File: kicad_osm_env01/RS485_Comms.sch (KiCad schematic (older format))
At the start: 13 parts, among them U7 ST3485EBDR

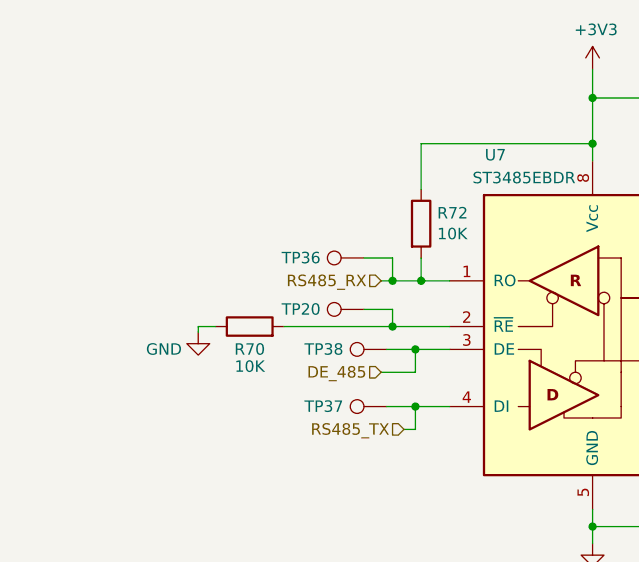
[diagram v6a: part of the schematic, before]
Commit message: updated schematics
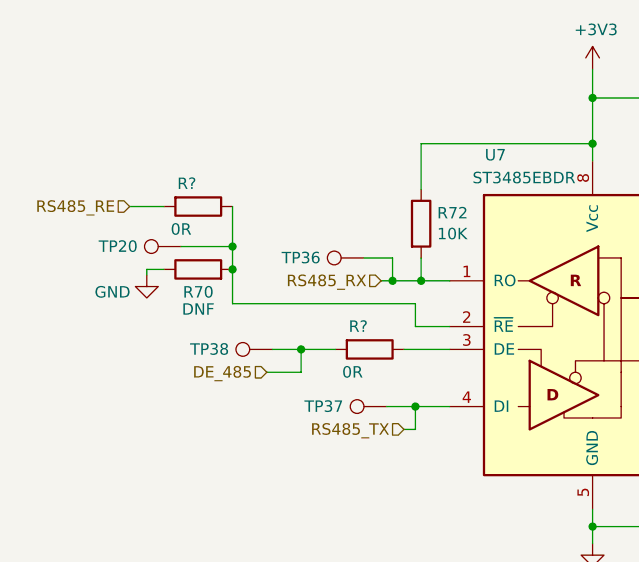
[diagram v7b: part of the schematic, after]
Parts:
- added R? (x2): 0R, symbol device:R
- R70: value 10K -> DNF
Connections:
- net DE_485: now also R?.2; no longer U7.3 (DE)
- net at R70.2, TP20.1, U7.2 (~RE): now also R?.1
- new net: R?.1, U7.3 (DE)
- new net RS485_RE: R?.2
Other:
- moved on the sheet: R70, TP20, TP38
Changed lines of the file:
@@
 L OSM_env01-rescue:R-device-ESP32-EVB_Rev_D-rescue R?
 U 1 1 609E7D1E
-P 4150 3825
+P 3925 3575
 AR Path="/609E7D1E" Ref="R?"  Part="1"
 AR Path="/609D4B87/609E7D1E" Ref="R70"  Part="1"
-F 0 "R70" V 4050 3825 50  0000 C CNN
-F 1 "10K" V 3975 3825 50  0000 C CNN
-F 2 "Resistor_SMD:R_0603_1608Metric" V 4080 3825 50  0001 C CNN
-F 3 "" H 4150 3825 50  0001 C CNN
-	1    4150 3825
+F 0 "R70" V 3825 3575 50  0000 C CNN
+F 1 "DNF" V 3750 3575 50  0000 C CNN
+F 2 "Resistor_SMD:R_0603_1608Metric" V 3855 3575 50  0001 C CNN
+F 3 "" H 3925 3575 50  0001 C CNN
+	1    3925 3575
 	0    -1   -1   0
 $EndComp
@@
 L OSM_env01-rescue:GND-ESP32-EVB_Rev_D #PWR?
 U 1 1 609E7D6C
-P 3925 3850
+P 3700 3600
 AR Path="/609E7D6C" Ref="#PWR?"  Part="1"
 AR Path="/609D4B87/609E7D6C" Ref="#PWR054"  Part="1"
-F 0 "#PWR054" H 3925 3600 50  0001 C CNN
-F 1 "GND" H 3775 3775 50  0000 C CNN
-F 2 "" H 3925 3850 60  0000 C CNN
-F 3 "" H 3925 3850 60  0000 C CNN
-	1    3925 3850
-	1    0    0    -1
-$EndComp
-Wire Wire Line
-	3925 3850 3925 3825
-Wire Wire Line
-	3925 3825 4000 3825
+F 0 "#PWR054" H 3700 3350 50  0001 C CNN
+F 1 "GND" H 3550 3525 50  0000 C CNN
+F 2 "" H 3700 3600 60  0000 C CNN
+F 3 "" H 3700 3600 60  0000 C CNN
+	1    3700 3600
+	1    0    0    -1
+$EndComp
+Wire Wire Line
+	3700 3600 3700 3575
+Wire Wire Line
+	3700 3575 3775 3575
 Wire Wire Line
 	4900 3025 5650 3025
@@
 L OSM_env01-rescue:Test_Point-Connector-ESP32-EVB_Rev_D-rescue TP?
 U 1 1 609E7D92
-P 4750 3925
+P 4250 3925
 AR Path="/609E7D92" Ref="TP?"  Part="1"
 AR Path="/609D4B87/609E7D92" Ref="TP38"  Part="1"
-F 0 "TP38" V 4750 4200 50  0000 C CNN
-F 1 "Test_Point" V 4675 4300 50  0001 C CNN
-F 2 "TestPoint:TestPoint_Pad_D1.5mm" H 4950 3925 50  0001 C CNN
-F 3 "~" H 4950 3925 50  0001 C CNN
-	1    4750 3925
+F 0 "TP38" V 4250 4200 50  0000 C CNN
+F 1 "Test_Point" V 4175 4300 50  0001 C CNN
+F 2 "TestPoint:TestPoint_Pad_D1.5mm" H 4450 3925 50  0001 C CNN
+F 3 "~" H 4450 3925 50  0001 C CNN
+	1    4250 3925
 	0    -1   -1   0
 $EndComp
@@
 Wire Wire Line
 	6950 4100 7025 4100
-Text HLabel 4725 4025 0    50   Input ~ 0
+Text HLabel 4225 4025 0    50   Input ~ 0
 DE_485
 Text HLabel 4725 3625 0    50   Input ~ 0
@@
 	4875 4175 5025 4175
 Wire Wire Line
-	4300 3825 4775 3825
-Wire Wire Line
-	4750 3925 4875 3925
-Wire Wire Line
-	4875 3925 4875 4025
-Wire Wire Line
-	4875 4025 4725 4025
-Connection ~ 4875 3925
-Wire Wire Line
-	4875 3925 5025 3925
+	4250 3925 4375 3925
+Wire Wire Line
+	4375 3925 4375 4025
+Wire Wire Line
+	4375 4025 4225 4025
+Connection ~ 4375 3925
+Wire Wire Line
+	4375 3925 4525 3925
 Text HLabel 4825 4275 0    50   Input ~ 0
 RS485_TX
@@
 L OSM_env01-rescue:Test_Point-Connector-ESP32-EVB_Rev_D-rescue TP?
 U 1 1 61C934C6
-P 4650 3750
+P 3850 3475
 AR Path="/61C934C6" Ref="TP?"  Part="1"
 AR Path="/609D4B87/61C934C6" Ref="TP20"  Part="1"
-F 0 "TP20" V 4650 4025 50  0000 C CNN
-F 1 "Test_Point" V 4775 4125 50  0001 C CNN
-F 2 "TestPoint:TestPoint_Pad_D1.5mm" H 4850 3750 50  0001 C CNN
-F 3 "~" H 4850 3750 50  0001 C CNN
-	1    4650 3750
-	0    -1   -1   0
-$EndComp
-Wire Wire Line
-	4650 3750 4775 3750
-Wire Wire Line
-	4775 3750 4775 3825
-Connection ~ 4775 3825
-Wire Wire Line
-	4775 3825 5025 3825
+F 0 "TP20" V 3850 3750 50  0000 C CNN
+F 1 "Test_Point" V 3975 3850 50  0001 C CNN
+F 2 "TestPoint:TestPoint_Pad_D1.5mm" H 4050 3475 50  0001 C CNN
+F 3 "~" H 4050 3475 50  0001 C CNN
+	1    3850 3475
+	0    -1   -1   0
+$EndComp
+Text HLabel 3625 3300 0    50   Input ~ 0
+RS485_RE
+Wire Wire Line
+	3775 3300 3625 3300
+Wire Wire Line
+	3850 3475 4075 3475
+Connection ~ 4075 3475
+$Comp
+L device:R R?
+U 1 1 614C78FA
+P 4675 3925
+AR Path="/6064BC1D/614C78FA" Ref="R?"  Part="1"
+AR Path="/609D4B87/614C78FA" Ref="R?"  Part="1"
+F 0 "R?" V 4575 3875 50  0000 C CNN
+F 1 "0R" V 4775 3850 50  0000 C CNN
+F 2 "" V 4605 3925 50  0001 C CNN
+F 3 "" H 4675 3925 50  0001 C CNN
+	1    4675 3925
+	0    1    1    0
+$EndComp
+$Comp
+L device:R R?
+U 1 1 614D39E0
+P 3925 3300
+AR Path="/6064BC1D/614D39E0" Ref="R?"  Part="1"
+AR Path="/609D4B87/614D39E0" Ref="R?"  Part="1"
+F 0 "R?" V 3825 3250 50  0000 C CNN
+F 1 "0R" V 4025 3225 50  0000 C CNN
+F 2 "" V 3855 3300 50  0001 C CNN
+F 3 "" H 3925 3300 50  0001 C CNN
+	1    3925 3300
+	0    1    1    0
+$EndComp
+Wire Wire Line
+	4075 3475 4075 3575
+Wire Wire Line
+	4075 3300 4075 3475
+Wire Wire Line
+	5025 3925 4825 3925
+Wire Wire Line
+	5025 3825 4875 3825
+Wire Wire Line
+	4875 3825 4875 3725
+Wire Wire Line
+	4075 3725 4075 3575
+Wire Wire Line
+	4075 3725 4875 3725
+Connection ~ 4075 3575
 $EndSCHEMATC

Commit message: updated schematics
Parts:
- gave numbers to parts that had none: 2
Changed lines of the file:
@@
 P 4675 3925
 AR Path="/6064BC1D/614C78FA" Ref="R?"  Part="1"
-AR Path="/609D4B87/614C78FA" Ref="R?"  Part="1"
-F 0 "R?" V 4575 3875 50  0000 C CNN
+AR Path="/609D4B87/614C78FA" Ref="R34"  Part="1"
+F 0 "R34" V 4575 3875 50  0000 C CNN
 F 1 "0R" V 4775 3850 50  0000 C CNN
 F 2 "" V 4605 3925 50  0001 C CNN
@@
 P 3925 3300
 AR Path="/6064BC1D/614D39E0" Ref="R?"  Part="1"
-AR Path="/609D4B87/614D39E0" Ref="R?"  Part="1"
-F 0 "R?" V 3825 3250 50  0000 C CNN
+AR Path="/609D4B87/614D39E0" Ref="R33"  Part="1"
+F 0 "R33" V 3825 3250 50  0000 C CNN
 F 1 "0R" V 4025 3225 50  0000 C CNN
 F 2 "" V 3855 3300 50  0001 C CNN
